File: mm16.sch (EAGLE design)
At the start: 57 parts, among them IC101 ATMEGA32-PU, IC102 DS1337, IC103 MAX483CPA, IC201 LTV847, IC202 LTV847, IC203 LTV847, IC204 LTV847, Q1 32,768kHz

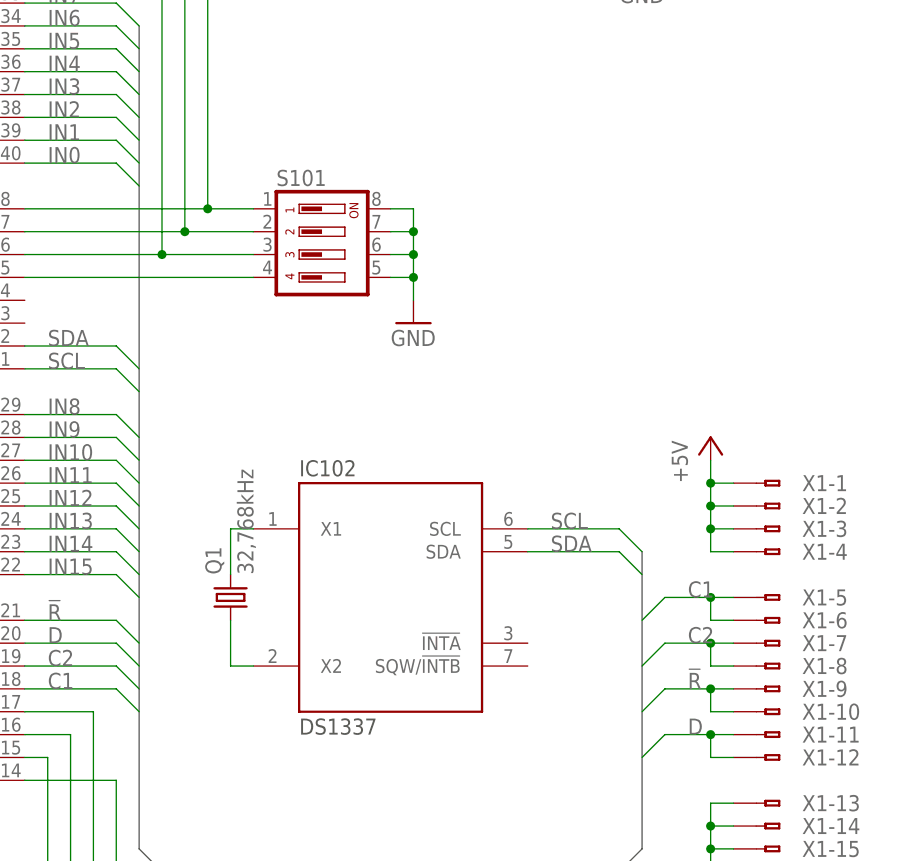
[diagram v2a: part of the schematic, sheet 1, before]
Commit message: Dipschalter durch Drehschalter ersetzt; 74HC594 durch 74HC595 ersetzt; Signalleitungen gedreht.
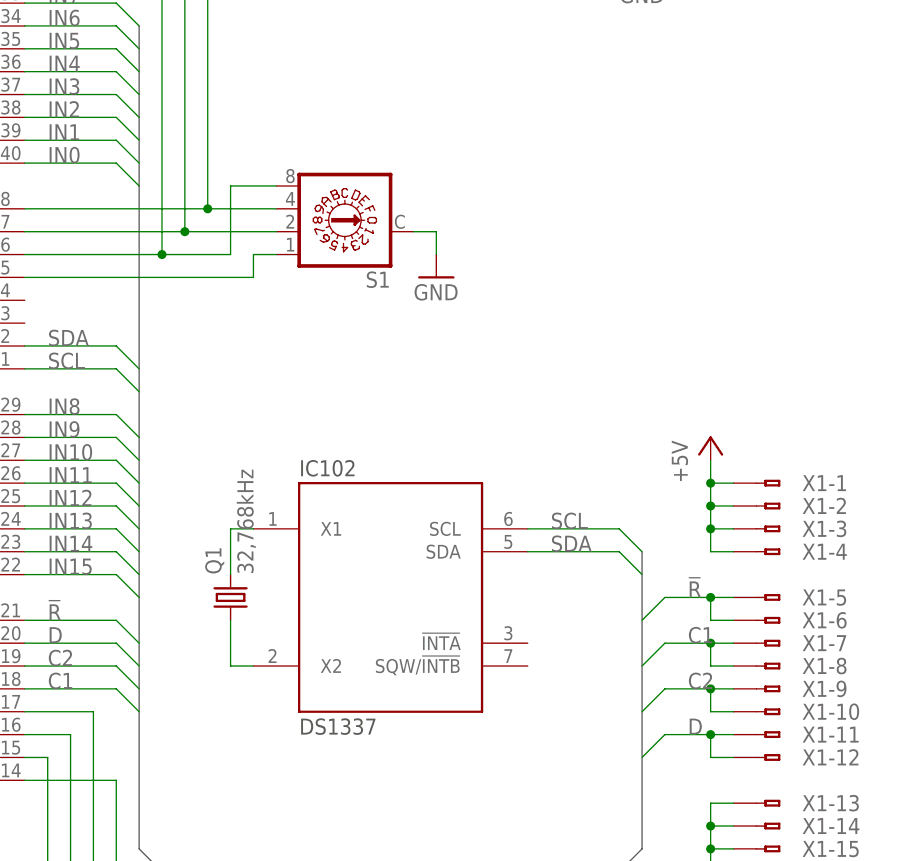
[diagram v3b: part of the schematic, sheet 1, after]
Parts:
- removed S101: (no value), schalter:DIP04YL
- added S1: (no value), switch-dil:P103
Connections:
- net !R: now also X1-5.A, X1-6.A; no longer X1-10.A, X1-9.A
- net C1: now also X1-7.A, X1-8.A; no longer X1-5.A, X1-6.A
- net C2: now also X1-10.A, X1-9.A; no longer X1-7.A, X1-8.A
- net GND: now also S1.C; no longer S101.5, S101.6, S101.7, S101.8
- net N$122: now also S1.8; no longer S101.3
- net N$123: now also S1.2; no longer S101.2
- net N$125: now also S1.4; no longer S101.1
- net N$130: now also S1.1; no longer S101.4
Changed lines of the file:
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@@
 <part name="GND43" library="versorgung" deviceset="GND" device=""/>
 <part name="GND44" library="versorgung" deviceset="GND" device=""/>
-<part name="S101" library="schalter" deviceset="DIP04YL" device=""/>
 <part name="IC102" library="ic-controller" deviceset="DS1337" device=""/>
 <part name="Q1" library="passiv" deviceset="Q_" device="HC49S" value="32,768kHz"/>
@@
 <part name="G1" library="battery" deviceset="CR2032V" device=""/>
 <part name="GND39" library="versorgung" deviceset="GND" device=""/>
+<part name="S1" library="switch-dil" deviceset="P103" device=""/>
 </parts>
 <sheets>
@@
 <instance part="GND42" gate="1" x="182.88" y="5.08"/>
 <instance part="GND43" gate="1" x="172.72" y="5.08"/>
-<instance part="GND44" gate="1" x="139.7" y="106.68"/>
-<instance part="S101" gate="1" x="129.54" y="116.84" rot="R270"/>
+<instance part="GND44" gate="1" x="142.24" y="111.76"/>
 <instance part="IC102" gate="G$1" x="137.16" y="76.2"/>
 <instance part="Q1" gate="G$1" x="119.38" y="76.2" rot="R90"/>
@@
 <instance part="G1" gate="1" x="218.44" y="152.4" rot="R90"/>
 <instance part="GND39" gate="1" x="218.44" y="144.78"/>
+<instance part="S1" gate="1" x="132.08" y="116.84" rot="R90"/>
 </instances>
 <busses>
@@
 <pinref part="GND43" gate="1" pin="GND"/>
 <wire x1="172.72" y1="12.7" x2="172.72" y2="7.62" width="0.1524" layer="91"/>
-</segment>
-<segment>
-<pinref part="GND44" gate="1" pin="GND"/>
-<wire x1="137.16" y1="111.76" x2="139.7" y2="111.76" width="0.1524" layer="91"/>
-<wire x1="139.7" y1="111.76" x2="139.7" y2="109.22" width="0.1524" layer="91"/>
-<wire x1="137.16" y1="114.3" x2="139.7" y2="114.3" width="0.1524" layer="91"/>
-<wire x1="139.7" y1="114.3" x2="139.7" y2="111.76" width="0.1524" layer="91"/>
-<junction x="139.7" y="111.76"/>
-<wire x1="137.16" y1="116.84" x2="139.7" y2="116.84" width="0.1524" layer="91"/>
-<wire x1="139.7" y1="116.84" x2="139.7" y2="114.3" width="0.1524" layer="91"/>
-<junction x="139.7" y="114.3"/>
-<wire x1="137.16" y1="119.38" x2="139.7" y2="119.38" width="0.1524" layer="91"/>
-<wire x1="139.7" y1="119.38" x2="139.7" y2="116.84" width="0.1524" layer="91"/>
-<junction x="139.7" y="116.84"/>
-<pinref part="S101" gate="1" pin="5"/>
-<pinref part="S101" gate="1" pin="6"/>
-<pinref part="S101" gate="1" pin="7"/>
-<pinref part="S101" gate="1" pin="8"/>
 </segment>
 <segment>
@@
 <pinref part="GND39" gate="1" pin="GND"/>
 </segment>
+<segment>
+<pinref part="S1" gate="1" pin="C"/>
+<pinref part="GND44" gate="1" pin="GND"/>
+<wire x1="139.7" y1="116.84" x2="142.24" y2="116.84" width="0.1524" layer="91"/>
+<wire x1="142.24" y1="116.84" x2="142.24" y2="114.3" width="0.1524" layer="91"/>
+</segment>
 </net>
 <net name="IN0" class="0">
@@
 <pinref part="IC101" gate="G$1" pin="(MOSI)PB5"/>
 <wire x1="111.76" y1="114.3" x2="96.52" y2="114.3" width="0.1524" layer="91"/>
-<wire x1="111.76" y1="114.3" x2="121.92" y2="114.3" width="0.1524" layer="91"/>
 <junction x="111.76" y="114.3"/>
-<pinref part="S101" gate="1" pin="3"/>
+<wire x1="111.76" y1="114.3" x2="119.38" y2="114.3" width="0.1524" layer="91"/>
+<wire x1="119.38" y1="114.3" x2="119.38" y2="121.92" width="0.1524" layer="91"/>
+<pinref part="S1" gate="1" pin="8"/>
+<wire x1="119.38" y1="121.92" x2="124.46" y2="121.92" width="0.1524" layer="91"/>
 </segment>
 </net>
@@
 <pinref part="IC101" gate="G$1" pin="(MISO)PB6"/>
 <wire x1="96.52" y1="116.84" x2="114.3" y2="116.84" width="0.1524" layer="91"/>
-<wire x1="114.3" y1="116.84" x2="121.92" y2="116.84" width="0.1524" layer="91"/>
 <junction x="114.3" y="116.84"/>
-<pinref part="S101" gate="1" pin="2"/>
+<pinref part="S1" gate="1" pin="2"/>
+<wire x1="114.3" y1="116.84" x2="124.46" y2="116.84" width="0.1524" layer="91"/>
 </segment>
 </net>
@@
 <pinref part="IC101" gate="G$1" pin="(SCK)PB7"/>
 <wire x1="116.84" y1="119.38" x2="96.52" y2="119.38" width="0.1524" layer="91"/>
-<wire x1="116.84" y1="119.38" x2="121.92" y2="119.38" width="0.1524" layer="91"/>
 <junction x="116.84" y="119.38"/>
-<pinref part="S101" gate="1" pin="1"/>
-</segment>
-</net>
-<net name="!R" class="0">
-<segment>
-<pinref part="IC101" gate="G$1" pin="(OC2)PD7"/>
-<wire x1="96.52" y1="73.66" x2="106.68" y2="73.66" width="0.1524" layer="91"/>
-<wire x1="106.68" y1="73.66" x2="109.22" y2="71.12" width="0.1524" layer="91"/>
-<label x="99.06" y="73.66" size="1.778" layer="95"/>
-</segment>
+<pinref part="S1" gate="1" pin="4"/>
+<wire x1="116.84" y1="119.38" x2="124.46" y2="119.38" width="0.1524" layer="91"/>
+</segment>
+</net>
+<net name="C2" class="0">
 <segment>
 <wire x1="175.26" y1="66.04" x2="172.72" y2="66.04" width="0.1524" layer="91"/>
@@
 <pinref part="X1" gate="-10" pin="A"/>
 </segment>
-</net>
-<net name="C2" class="0">
 <segment>
 <pinref part="IC101" gate="G$1" pin="(OC1A)PD5"/>
@@
 <label x="99.06" y="68.58" size="1.778" layer="95"/>
 </segment>
+</net>
+<net name="C1" class="0">
 <segment>
 <wire x1="175.26" y1="71.12" x2="172.72" y2="71.12" width="0.1524" layer="91"/>
@@
 <pinref part="X1" gate="-8" pin="A"/>
 </segment>
-</net>
-<net name="C1" class="0">
 <segment>
 <pinref part="IC101" gate="G$1" pin="(OC1B)PD4"/>
@@
 <label x="99.06" y="66.04" size="1.778" layer="95"/>
 </segment>
+</net>
+<net name="!R" class="0">
 <segment>
 <wire x1="175.26" y1="76.2" x2="172.72" y2="76.2" width="0.1524" layer="91"/>
@@
 <pinref part="X1" gate="-6" pin="A"/>
 </segment>
+<segment>
+<pinref part="IC101" gate="G$1" pin="(OC2)PD7"/>
+<wire x1="96.52" y1="73.66" x2="106.68" y2="73.66" width="0.1524" layer="91"/>
+<wire x1="106.68" y1="73.66" x2="109.22" y2="71.12" width="0.1524" layer="91"/>
+<label x="99.06" y="73.66" size="1.778" layer="95"/>
+</segment>
 </net>
 <net name="D" class="0">
-<segment>
-<pinref part="IC101" gate="G$1" pin="(ICP)PD6"/>
-<wire x1="96.52" y1="71.12" x2="106.68" y2="71.12" width="0.1524" layer="91"/>
-<wire x1="106.68" y1="71.12" x2="109.22" y2="68.58" width="0.1524" layer="91"/>
-<label x="99.06" y="71.12" size="1.778" layer="95"/>
-</segment>
 <segment>
 <wire x1="175.26" y1="60.96" x2="172.72" y2="60.96" width="0.1524" layer="91"/>
@@
 <pinref part="X1" gate="-12" pin="A"/>
 </segment>
+<segment>
+<pinref part="IC101" gate="G$1" pin="(ICP)PD6"/>
+<wire x1="96.52" y1="71.12" x2="106.68" y2="71.12" width="0.1524" layer="91"/>
+<wire x1="106.68" y1="71.12" x2="109.22" y2="68.58" width="0.1524" layer="91"/>
+<label x="99.06" y="71.12" size="1.778" layer="95"/>
+</segment>
 </net>
 <net name="N$63" class="0">
@@
 <pinref part="IC101" gate="G$1" pin="(SS)PB4"/>
 <wire x1="96.52" y1="111.76" x2="121.92" y2="111.76" width="0.1524" layer="91"/>
-<pinref part="S101" gate="1" pin="4"/>
-</segment>
-</net>
+<wire x1="121.92" y1="111.76" x2="121.92" y2="114.3" width="0.1524" layer="91"/>
+<wire x1="121.92" y1="114.3" x2="124.46" y2="114.3" width="0.1524" layer="91"/>
+<pinref part="S1" gate="1" pin="1"/>
+</segment>
+</net>

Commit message: Anschlüsse neu possitioniert und Bohrungen hinzugefügt
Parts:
- X4: device anschluss:WAGO_236-402 -> anschluss:WAGO_236-401
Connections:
- net GNDIO: now also X4.A, X4.B; no longer X4.1.A, X4.1.B, X4.2.A, X4.2.B
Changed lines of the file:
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@@
 <part name="GND34" library="versorgung" deviceset="GNDIO" device=""/>
 <part name="GND38" library="versorgung" deviceset="GNDIO" device=""/>
-<part name="X4" library="anschluss" deviceset="WAGO_236-402" device=""/>
 <part name="X5" library="anschluss" deviceset="WAGO_236-402" device=""/>
 <part name="X6" library="anschluss" deviceset="WAGO_236-402" device=""/>
@@
 <part name="GND39" library="versorgung" deviceset="GND" device=""/>
 <part name="S1" library="switch-dil" deviceset="P103" device=""/>
+<part name="X4" library="anschluss" deviceset="WAGO_236-401" device=""/>
 </parts>
 <sheets>
@@
 <instance part="GND38" gate="G$1" x="165.1" y="38.1"/>
 <instance part="X4" gate=".1" x="68.58" y="167.64"/>
-<instance part="X4" gate=".2" x="157.48" y="167.64"/>
 </instances>
 <busses>
@@
 </segment>
 <segment>
-<wire x1="73.66" y1="167.64" x2="76.2" y2="167.64" width="0.1524" layer="91"/>
-<pinref part="X4" gate=".1" pin="A"/>
 <pinref part="GND10" gate="G$1" pin="GNDIO"/>
 <wire x1="76.2" y1="165.1" x2="76.2" y2="167.64" width="0.1524" layer="91"/>
+<pinref part="R201" gate="G$1" pin="1"/>
+<wire x1="76.2" y1="167.64" x2="78.74" y2="167.64" width="0.1524" layer="91"/>
+<pinref part="X4" gate=".1" pin="A"/>
+<wire x1="76.2" y1="167.64" x2="73.66" y2="167.64" width="0.1524" layer="91"/>
+<junction x="76.2" y="167.64"/>
 <pinref part="X4" gate=".1" pin="B"/>
 <wire x1="73.66" y1="167.64" x2="71.12" y2="167.64" width="0.1524" layer="91"/>
-<pinref part="R201" gate="G$1" pin="1"/>
-<wire x1="76.2" y1="167.64" x2="78.74" y2="167.64" width="0.1524" layer="91"/>
-<junction x="76.2" y="167.64"/>
 </segment>
 <segment>
 <pinref part="R209" gate="G$1" pin="1"/>
-<wire x1="162.56" y1="167.64" x2="165.1" y2="167.64" width="0.1524" layer="91"/>
-<pinref part="X4" gate=".2" pin="A"/>
 <pinref part="GND28" gate="G$1" pin="GNDIO"/>
 <wire x1="165.1" y1="167.64" x2="167.64" y2="167.64" width="0.1524" layer="91"/>
 <wire x1="165.1" y1="165.1" x2="165.1" y2="167.64" width="0.1524" layer="91"/>
-<junction x="165.1" y="167.64"/>
-<pinref part="X4" gate=".2" pin="B"/>
-<wire x1="162.56" y1="167.64" x2="160.02" y2="167.64" width="0.1524" layer="91"/>
-</segment>
-</net>
+</segment>
+</net>

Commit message: Alarme angeschlossen; Detailverbesserungen am Layout
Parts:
- Q1: device passiv:Q_HC49S -> passiv:Q_TC38H
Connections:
- new net ALARM1: IC101.(AIN1/OC0)PB3, IC102G$1.!INTA
- new net ALARM2: IC101.(AIN0/INT2)PB2, IC102G$1.SQW/!INTB
- net +5V: now also SV101.VCC
- net N$126: now also Q1.1; no longer Q1.2
- net N$127: now also Q1.2; no longer Q1.1
- net VCC: no longer SV101.VCC
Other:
- moved on the sheet: Q1
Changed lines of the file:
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@@
 <part name="GND44" library="versorgung" deviceset="GND" device=""/>
 <part name="IC102" library="ic-controller" deviceset="DS1337" device=""/>
-<part name="Q1" library="passiv" deviceset="Q_" device="HC49S" value="32,768kHz"/>
+<part name="Q1" library="passiv" deviceset="Q_" device="TC38H" value="32,768kHz"/>
 <part name="C1" library="passiv" deviceset="C_" device="025-025X050" value="10nF"/>
 <part name="GND45" library="versorgung" deviceset="GND" device=""/>
@@
 <part name="X1" library="anschluss" deviceset="WS16" device="V"/>
 <part name="P+7" library="versorgung" deviceset="VCC" device="" value="VBAT"/>
-<part name="P+2" library="versorgung" deviceset="VCC" device="" value="VBAT"/>
 <part name="P+8" library="versorgung" deviceset="VCC" device="" value="VBAT"/>
 <part name="P+9" library="versorgung" deviceset="VCC" device="" value="VBAT"/>
@@
 <part name="S1" library="switch-dil" deviceset="P103" device=""/>
 <part name="X4" library="anschluss" deviceset="WAGO_236-401" device=""/>
+<part name="P+2" library="versorgung" deviceset="+5V" device=""/>
 </parts>
 <sheets>
@@
 <instance part="GND44" gate="1" x="142.24" y="111.76"/>
 <instance part="IC102" gate="G$1" x="137.16" y="76.2"/>
-<instance part="Q1" gate="G$1" x="119.38" y="76.2" rot="R90"/>
+<instance part="Q1" gate="G$1" x="119.38" y="76.2" rot="R270"/>
 <instance part="IC102" gate="P" x="210.82" y="15.24"/>
 <instance part="C1" gate="G$1" x="200.66" y="17.78"/>
@@
 <instance part="X1" gate="-16" x="180.34" y="45.72" rot="R180"/>
 <instance part="P+7" gate="VCC" x="187.96" y="165.1"/>
-<instance part="P+2" gate="VCC" x="86.36" y="167.64"/>
 <instance part="P+8" gate="VCC" x="210.82" y="25.4"/>
 <instance part="P+9" gate="VCC" x="200.66" y="25.4"/>
@@
 <instance part="GND39" gate="1" x="218.44" y="144.78"/>
 <instance part="S1" gate="1" x="132.08" y="116.84" rot="R90"/>
+<instance part="P+2" gate="1" x="86.36" y="167.64"/>
 </instances>
 <busses>
-<bus name="IN[0..15],OUT[0..15],C1,C2,D,!R,SCL,SDA">
+<bus name="IN[0..15],C1,C2,D,!R,SCL,SDA,ALARM1,ALARM2">
 <segment>
 <wire x1="116.84" y1="40.64" x2="109.22" y2="48.26" width="0.762" layer="92"/>
@@
 <pinref part="X1" gate="-4" pin="A"/>
 </segment>
+<segment>
+<pinref part="SV101" gate="1" pin="VCC"/>
+<wire x1="86.36" y1="165.1" x2="86.36" y2="160.02" width="0.1524" layer="91"/>
+<wire x1="86.36" y1="160.02" x2="83.82" y2="160.02" width="0.1524" layer="91"/>
+<pinref part="P+2" gate="1" pin="+5V"/>
+</segment>
 </net>
 <net name="N$42" class="0">
@@
 <segment>
 <pinref part="IC102" gate="G$1" pin="X1"/>
-<pinref part="Q1" gate="G$1" pin="2"/>
 <wire x1="121.92" y1="83.82" x2="119.38" y2="83.82" width="0.1524" layer="91"/>
+<pinref part="Q1" gate="G$1" pin="1"/>
 <wire x1="119.38" y1="83.82" x2="119.38" y2="78.74" width="0.1524" layer="91"/>
 </segment>
@@
 <net name="N$127" class="0">
 <segment>
-<pinref part="Q1" gate="G$1" pin="1"/>
-<wire x1="119.38" y1="73.66" x2="119.38" y2="68.58" width="0.1524" layer="91"/>
 <pinref part="IC102" gate="G$1" pin="X2"/>
 <wire x1="119.38" y1="68.58" x2="121.92" y2="68.58" width="0.1524" layer="91"/>
+<pinref part="Q1" gate="G$1" pin="2"/>
+<wire x1="119.38" y1="73.66" x2="119.38" y2="68.58" width="0.1524" layer="91"/>
 </segment>
 </net>
@@
 </net>
 <net name="VCC" class="0">
-<segment>
-<pinref part="SV101" gate="1" pin="VCC"/>
-<wire x1="86.36" y1="165.1" x2="86.36" y2="160.02" width="0.1524" layer="91"/>
-<wire x1="86.36" y1="160.02" x2="83.82" y2="160.02" width="0.1524" layer="91"/>
-<pinref part="P+2" gate="VCC" pin="VCC"/>
-</segment>
 <segment>
 <pinref part="IC102" gate="P" pin="VCC"/>
@@
 </segment>
 </net>
+<net name="ALARM1" class="0">
+<segment>
+<pinref part="IC102" gate="G$1" pin="!INTA"/>
+<wire x1="152.4" y1="71.12" x2="162.56" y2="71.12" width="0.1524" layer="91"/>
+<wire x1="162.56" y1="71.12" x2="165.1" y2="68.58" width="0.1524" layer="91"/>
+<label x="154.94" y="71.12" size="1.778" layer="95"/>
+</segment>
+<segment>
+<pinref part="IC101" gate="G$1" pin="(AIN1/OC0)PB3"/>
+<wire x1="96.52" y1="109.22" x2="106.68" y2="109.22" width="0.1524" layer="91"/>
+<wire x1="106.68" y1="109.22" x2="109.22" y2="106.68" width="0.1524" layer="91"/>
+<label x="99.06" y="109.22" size="1.778" layer="95"/>
+</segment>
+</net>
+<net name="ALARM2" class="0">
+<segment>
+<pinref part="IC101" gate="G$1" pin="(AIN0/INT2)PB2"/>
+<wire x1="96.52" y1="106.68" x2="106.68" y2="106.68" width="0.1524" layer="91"/>
+<wire x1="106.68" y1="106.68" x2="109.22" y2="104.14" width="0.1524" layer="91"/>
+<label x="99.06" y="106.68" size="1.778" layer="95"/>
+</segment>
+<segment>
+<pinref part="IC102" gate="G$1" pin="SQW/!INTB"/>
+<wire x1="152.4" y1="68.58" x2="162.56" y2="68.58" width="0.1524" layer="91"/>
+<wire x1="162.56" y1="68.58" x2="165.1" y2="66.04" width="0.1524" layer="91"/>
+<label x="154.94" y="68.58" size="1.778" layer="95"/>
+</segment>
+</net>
